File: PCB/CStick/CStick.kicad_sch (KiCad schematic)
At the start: 6 parts, among them J1 Conn_01x04_Male, U1 Stickbox_Assembly

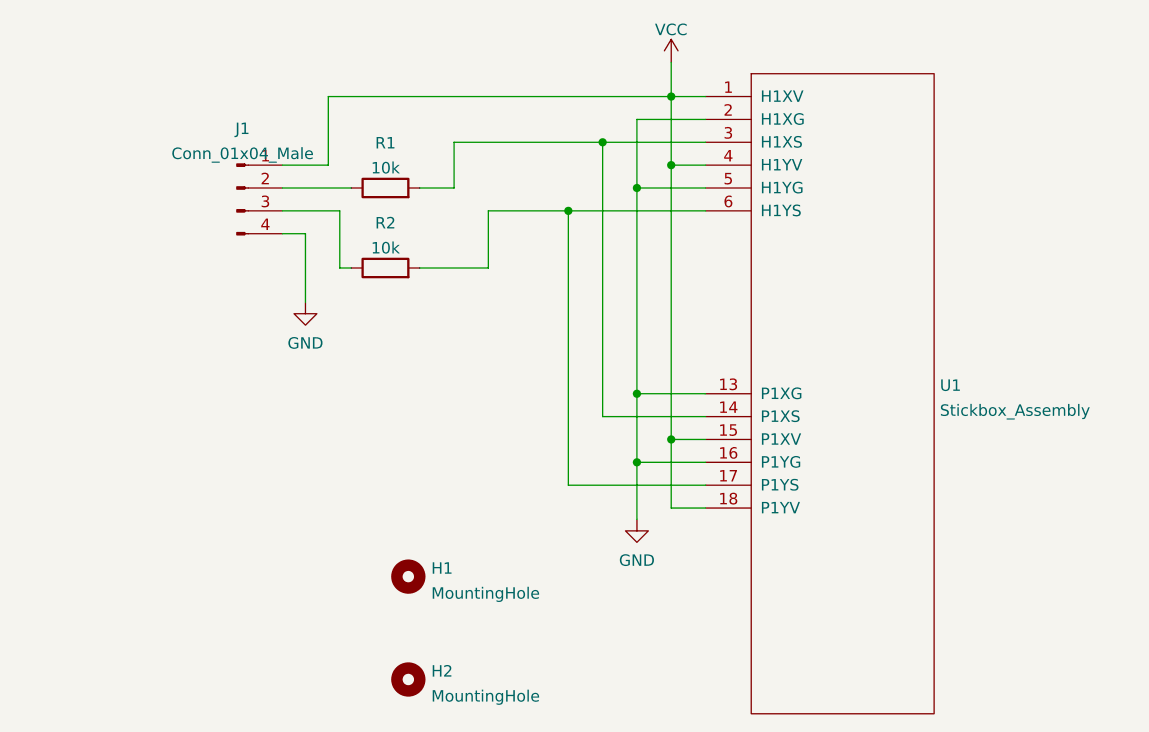
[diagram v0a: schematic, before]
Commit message: Changed PCB folder structure to sperate Motherboard from Cstick board, updated the diode part number for JLC to one that is in stock
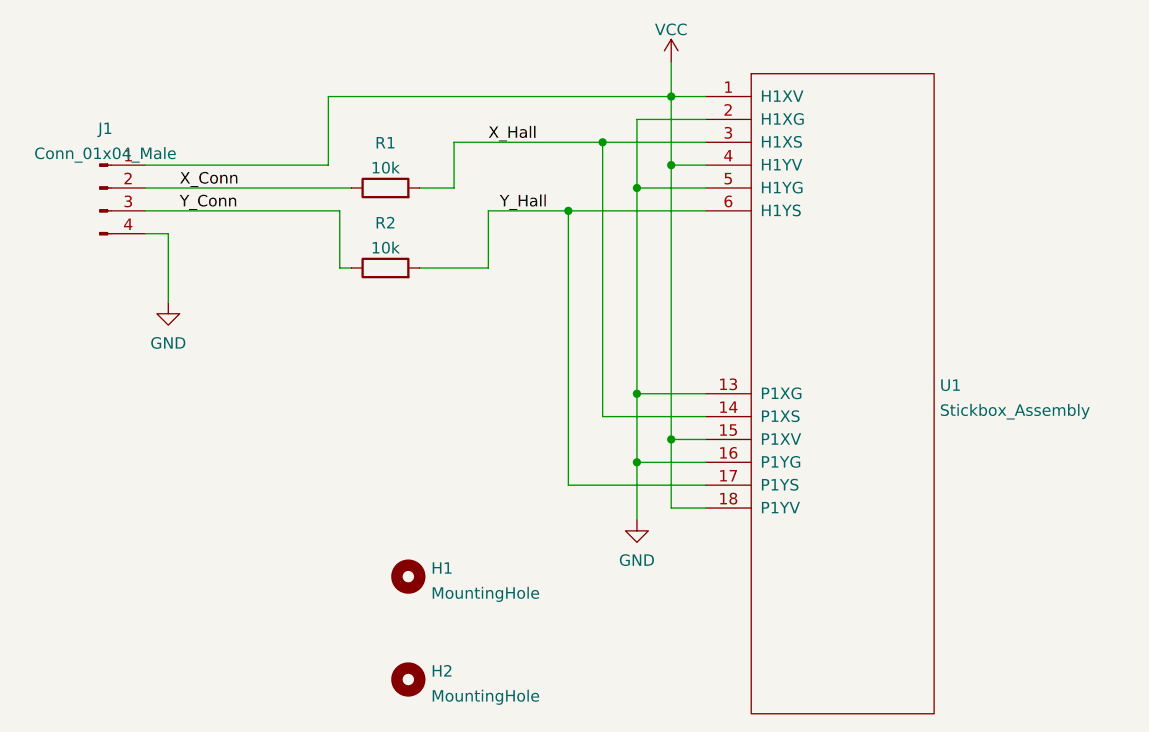
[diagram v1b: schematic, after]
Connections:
- net X_Conn: now reaches J1.2 (Pin_2), R1.1
- net X_Hall: now reaches R1.2, U1.14 (P1XS), U1.3 (H1XS)
- net Y_Conn: now reaches J1.3 (Pin_3), R2.1
- net Y_Hall: now reaches R2.2, U1.17 (P1YS), U1.6 (H1YS)
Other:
- moved on the sheet: J1
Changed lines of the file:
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@@
     (stroke (width 0) (type default) (color 0 0 0 0))
   )
-  (wire (pts (xy 77.47 77.47) (xy 80.01 77.47))
+  (wire (pts (xy 62.23 77.47) (xy 64.77 77.47))
     (stroke (width 0) (type default) (color 0 0 0 0))
   )
@@
     (stroke (width 0) (type default) (color 0 0 0 0))
   )
-  (wire (pts (xy 77.47 69.85) (xy 82.55 69.85))
+  (wire (pts (xy 62.23 69.85) (xy 82.55 69.85))
     (stroke (width 0) (type default) (color 0 0 0 0))
   )
@@
     (stroke (width 0) (type default) (color 0 0 0 0))
   )
-  (wire (pts (xy 77.47 72.39) (xy 85.09 72.39))
+  (wire (pts (xy 62.23 72.39) (xy 85.09 72.39))
     (stroke (width 0) (type default) (color 0 0 0 0))
   )
@@
     (stroke (width 0) (type default) (color 0 0 0 0))
   )
-  (wire (pts (xy 80.01 77.47) (xy 80.01 85.09))
+  (wire (pts (xy 64.77 77.47) (xy 64.77 85.09))
     (stroke (width 0) (type default) (color 0 0 0 0))
   )
-  (wire (pts (xy 77.47 74.93) (xy 83.82 74.93))
+  (wire (pts (xy 62.23 74.93) (xy 83.82 74.93))
     (stroke (width 0) (type default) (color 0 0 0 0))
   )
@@
   (wire (pts (xy 83.82 81.28) (xy 85.09 81.28))
     (stroke (width 0) (type default) (color 0 0 0 0))
+  )
+  (label "X_Hall" (at 100.33 67.31 0)
+    (effects (font (size 1.27 1.27)) (justify left bottom))
+  )
+  (label "Y_Hall" (at 101.6 74.93 0)
+    (effects (font (size 1.27 1.27)) (justify left bottom))
+  )
+  (label "X_Conn" (at 66.04 72.39 0)
+    (effects (font (size 1.27 1.27)) (justify left bottom))
+  )
+  (label "Y_Conn" (at 66.04 74.93 0)
+    (effects (font (size 1.27 1.27)) (justify left bottom))
   )
   (symbol (lib_id "Device:R") (at 88.9 72.39 90) (unit 1)
@@
     (pin "2")
   )
-  (symbol (lib_id "power:GND") (at 80.01 85.09 0) (unit 1)
+  (symbol (lib_id "power:GND") (at 64.77 85.09 0) (unit 1)
     (in_bom yes) (on_board yes) (fields_autoplaced)
-    (property "Reference" "#PWR01" (id 0) (at 80.01 91.44 0)
+    (property "Reference" "#PWR01" (id 0) (at 64.77 91.44 0)
       (effects (font (size 1.27 1.27)) hide)
     )
-    (property "Value" "GND" (id 1) (at 80.01 89.6525 0))
-    (property "Footprint" "" (id 2) (at 80.01 85.09 0)
+    (property "Value" "GND" (id 1) (at 64.77 89.6525 0))
+    (property "Footprint" "" (id 2) (at 64.77 85.09 0)
       (effects (font (size 1.27 1.27)) hide)
     )
-    (property "Datasheet" "" (id 3) (at 80.01 85.09 0)
+    (property "Datasheet" "" (id 3) (at 64.77 85.09 0)
       (effects (font (size 1.27 1.27)) hide)
     )
@@
     (pin "2")
   )
-  (symbol (lib_id "Connector:Conn_01x04_Male") (at 72.39 72.39 0) (unit 1)
+  (symbol (lib_id "Connector:Conn_01x04_Male") (at 57.15 72.39 0) (unit 1)
     (in_bom yes) (on_board yes) (fields_autoplaced)
-    (property "Reference" "J1" (id 0) (at 73.025 65.8073 0))
-    (property "Value" "Conn_01x04_Male" (id 1) (at 73.025 68.5824 0))
-    (property "Footprint" "Connector_PinHeader_2.00mm:PinHeader_1x04_P2.00mm_Vertical" (id 2) (at 72.39 72.39 0)
+    (property "Reference" "J1" (id 0) (at 57.785 65.8073 0))
+    (property "Value" "Conn_01x04_Male" (id 1) (at 57.785 68.5824 0))
+    (property "Footprint" "Connector_PinHeader_2.00mm:PinHeader_1x04_P2.00mm_Vertical" (id 2) (at 57.15 72.39 0)
       (effects (font (size 1.27 1.27)) hide)
     )
-    (property "Datasheet" "~" (id 3) (at 72.39 72.39 0)
+    (property "Datasheet" "~" (id 3) (at 57.15 72.39 0)
       (effects (font (size 1.27 1.27)) hide)
     )
